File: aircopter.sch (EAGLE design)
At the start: 43 parts, among them IC1 STF202-22T1G, M1 WIRELESS-NRF24L01, U2 GY-521MPU6050, Y1 20 MHz

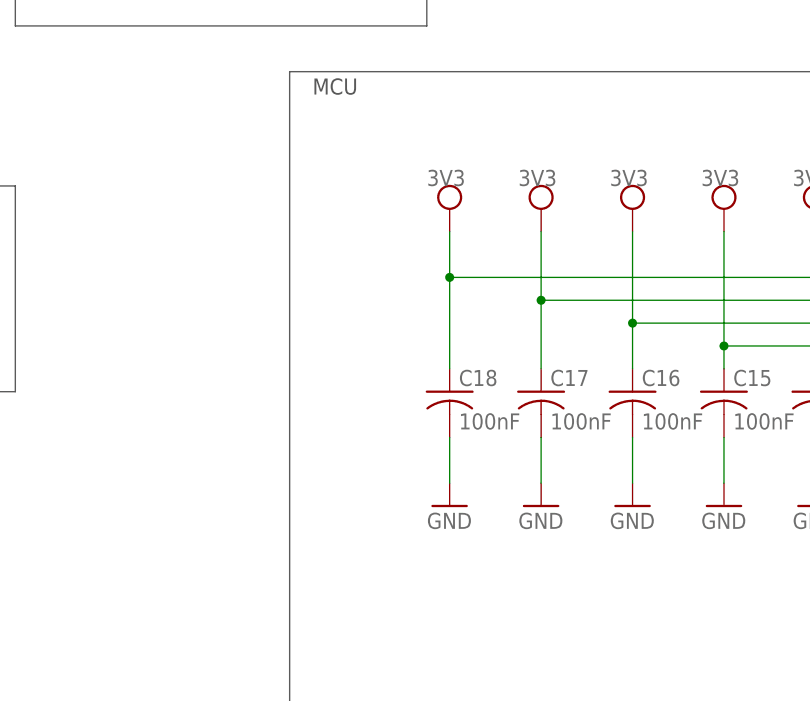
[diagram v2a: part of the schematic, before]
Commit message: minor fix to mcu
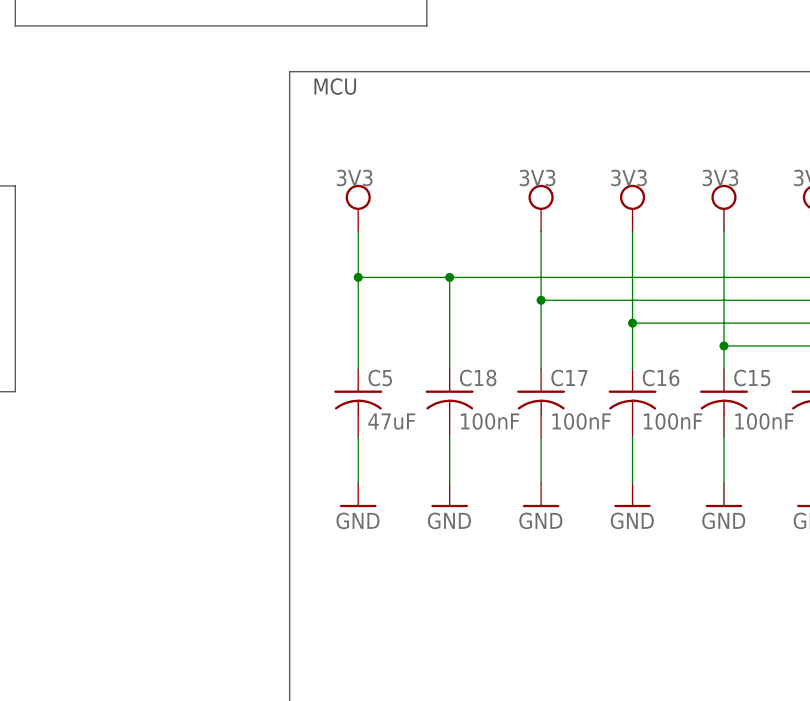
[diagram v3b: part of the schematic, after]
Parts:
- added C5: 47uF, rcl:C-USC0603
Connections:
- net 3V3: now also C5.1
- net GND: now also C5.2
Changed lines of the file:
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@@
 <part name="GND22" library="IR_Sensor" deviceset="SUPPLY1_GND" device=""/>
 <part name="TX/RX" library="pinhead" library_urn="urn:adsk.eagle:library:325" deviceset="PINHD-1X2" device="" package3d_urn="urn:adsk.eagle:package:22435/2"/>
+<part name="C5" library="rcl" library_urn="urn:adsk.eagle:library:334" deviceset="C-US" device="C0603" package3d_urn="urn:adsk.eagle:package:23616/2" value="47uF"/>
+<part name="GND9" library="IR_Sensor" deviceset="SUPPLY1_GND" device=""/>
 </parts>
 <sheets>
@@
 <instance part="GND20" gate="1" x="5.08" y="-132.08" smashed="yes"/>
 <instance part="GND21" gate="1" x="15.24" y="-132.08" smashed="yes"/>
-<instance part="SUPPLY3" gate="G$1" x="-25.4" y="-99.06" smashed="yes"/>
+<instance part="SUPPLY3" gate="G$1" x="-35.56" y="-99.06" smashed="yes"/>
 <instance part="SUPPLY8" gate="G$1" x="-15.24" y="-99.06" smashed="yes"/>
 <instance part="SUPPLY9" gate="G$1" x="-5.08" y="-99.06" smashed="yes"/>
@@
 <attribute name="VALUE" x="-87.63" y="-114.3" size="1.778" layer="96"/>
 </instance>
+<instance part="C5" gate="G$1" x="-35.56" y="-119.38" smashed="yes">
+<attribute name="NAME" x="-34.544" y="-118.745" size="1.778" layer="95"/>
+<attribute name="VALUE" x="-34.544" y="-123.571" size="1.778" layer="96"/>
+</instance>
+<instance part="GND9" gate="1" x="-35.56" y="-132.08" smashed="yes"/>
 </instances>
 <busses>
@@
 <label x="27.94" y="-210.82" size="1.778" layer="95"/>
 </segment>
+<segment>
+<pinref part="C5" gate="G$1" pin="2"/>
+<pinref part="GND9" gate="1" pin="GND"/>
+<wire x1="-35.56" y1="-124.46" x2="-35.56" y2="-129.54" width="0.1524" layer="91"/>
+<label x="-38.1" y="-134.62" size="1.778" layer="95"/>
+</segment>
 </net>
 <net name="N$2" class="0">
@@
 <pinref part="U$7" gate="G$1" pin="VDD@1"/>
 <wire x1="33.02" y1="-106.68" x2="-25.4" y2="-106.68" width="0.1524" layer="91"/>
+<wire x1="-25.4" y1="-106.68" x2="-35.56" y2="-106.68" width="0.1524" layer="91"/>
+<wire x1="-35.56" y1="-106.68" x2="-35.56" y2="-101.6" width="0.1524" layer="91"/>
+<junction x="-35.56" y="-106.68"/>
+<pinref part="SUPPLY3" gate="G$1" pin="+V"/>
+<label x="-38.1" y="-96.52" size="1.778" layer="95"/>
+<pinref part="C5" gate="G$1" pin="1"/>
+<wire x1="-35.56" y1="-106.68" x2="-35.56" y2="-116.84" width="0.1524" layer="91"/>
 <pinref part="C18" gate="G$1" pin="1"/>
-<wire x1="-25.4" y1="-106.68" x2="-25.4" y2="-116.84" width="0.1524" layer="91"/>
-<wire x1="-25.4" y1="-106.68" x2="-25.4" y2="-101.6" width="0.1524" layer="91"/>
+<wire x1="-25.4" y1="-116.84" x2="-25.4" y2="-106.68" width="0.1524" layer="91"/>
 <junction x="-25.4" y="-106.68"/>
-<pinref part="SUPPLY3" gate="G$1" pin="+V"/>
-<label x="-27.94" y="-96.52" size="1.778" layer="95"/>
-</segment>
-</net>
+</segment>
+</net>
